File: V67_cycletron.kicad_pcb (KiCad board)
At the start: 4 copper layers, 107.8 x 44.1 mm, 54 parts, among them J1 USB_C_Receptacle_USB2.0_16P, J2 Conn_01x04_Socket, J3 Conn_01x04_Socket, U2 LM1117DT-3.3, U3 L7805, U4 ESP32-S3-WROOM-1

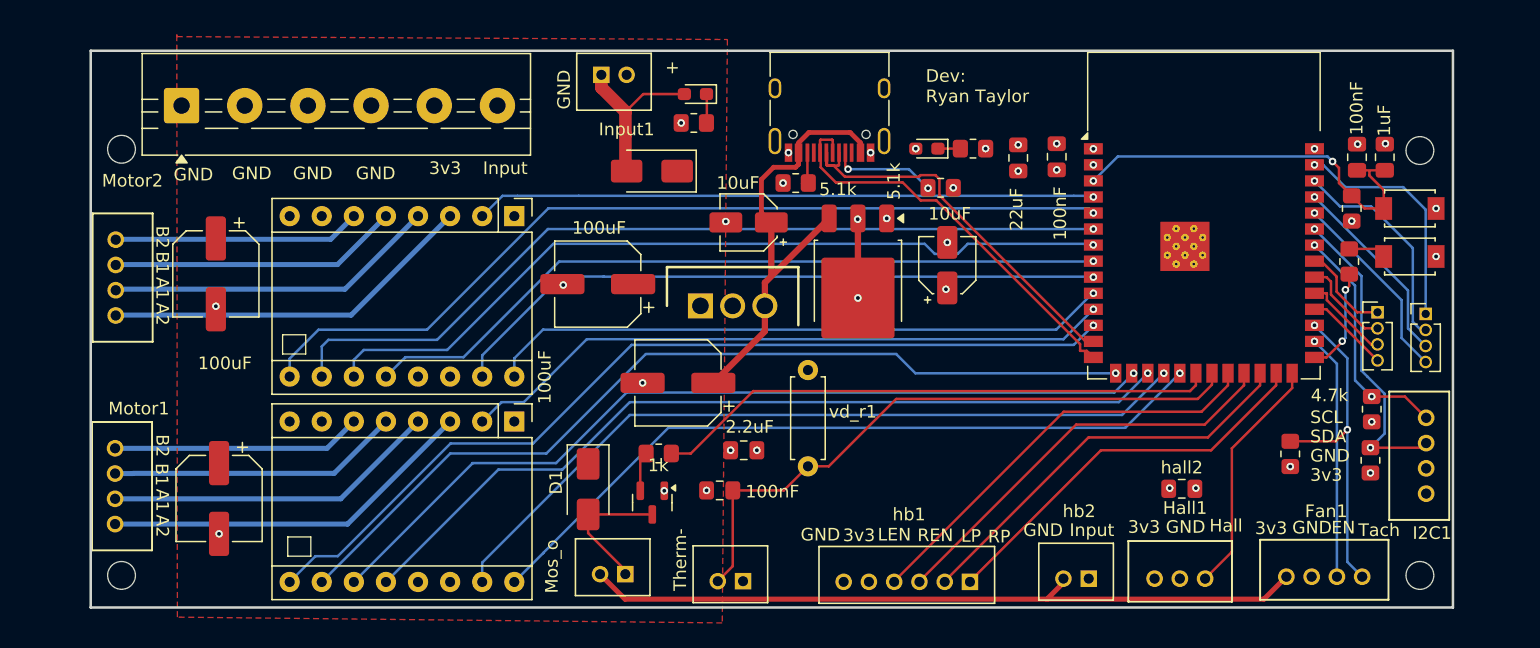
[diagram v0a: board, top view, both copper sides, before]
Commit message: change moving parts for reorder
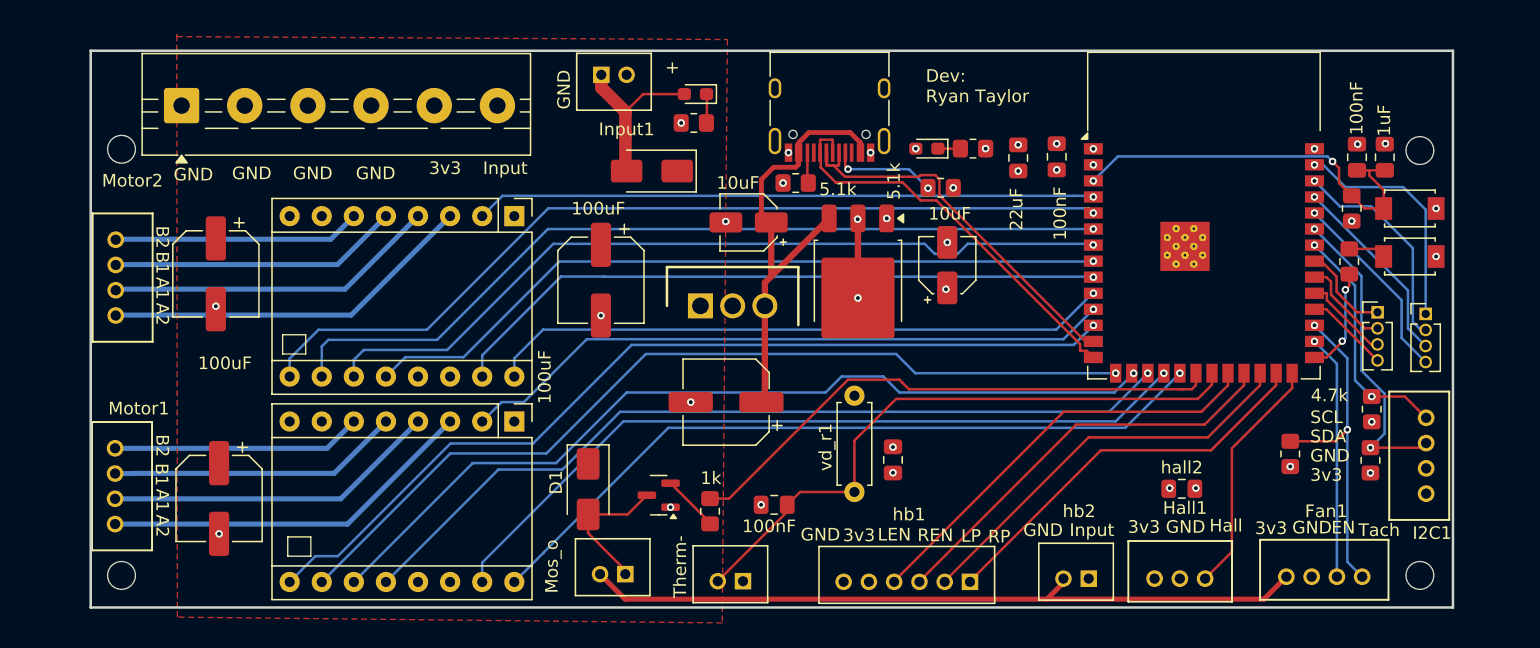
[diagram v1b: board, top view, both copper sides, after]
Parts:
- moved vd_c1 11.8 mm to (103.9, 104.9), turned to 90 degrees
- moved tr3 6.12 mm to (89.4, 109.0), turned to -90 degrees
- moved vd_c2 4.47 mm to (94.5, 108.5)
- moved vd_r1 4.21 mm to (100.8, 107.4)
- moved 3v3in1 4.10 mm to (90.7, 100.3)
- moved mosfet4 0.78 mm to (85.3, 107.7), turned to 180 degrees
- moved 5Vin1 0.40 mm to (80.8, 90.7), turned to -90 degrees
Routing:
- net Net-(mosfet4-G): track 3.31 -> 4.93 mm
- net Motor1_M1: track 68.6 -> 69.6 mm
- net mosfet1_i: track 44.7 -> 43.8 mm
- net Therm-: track 50.1 -> 49.3 mm
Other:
- board text removed: "2.2uF"

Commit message: updated for 3rd time, lcsc numbers for cap were through hole not smd, fixed
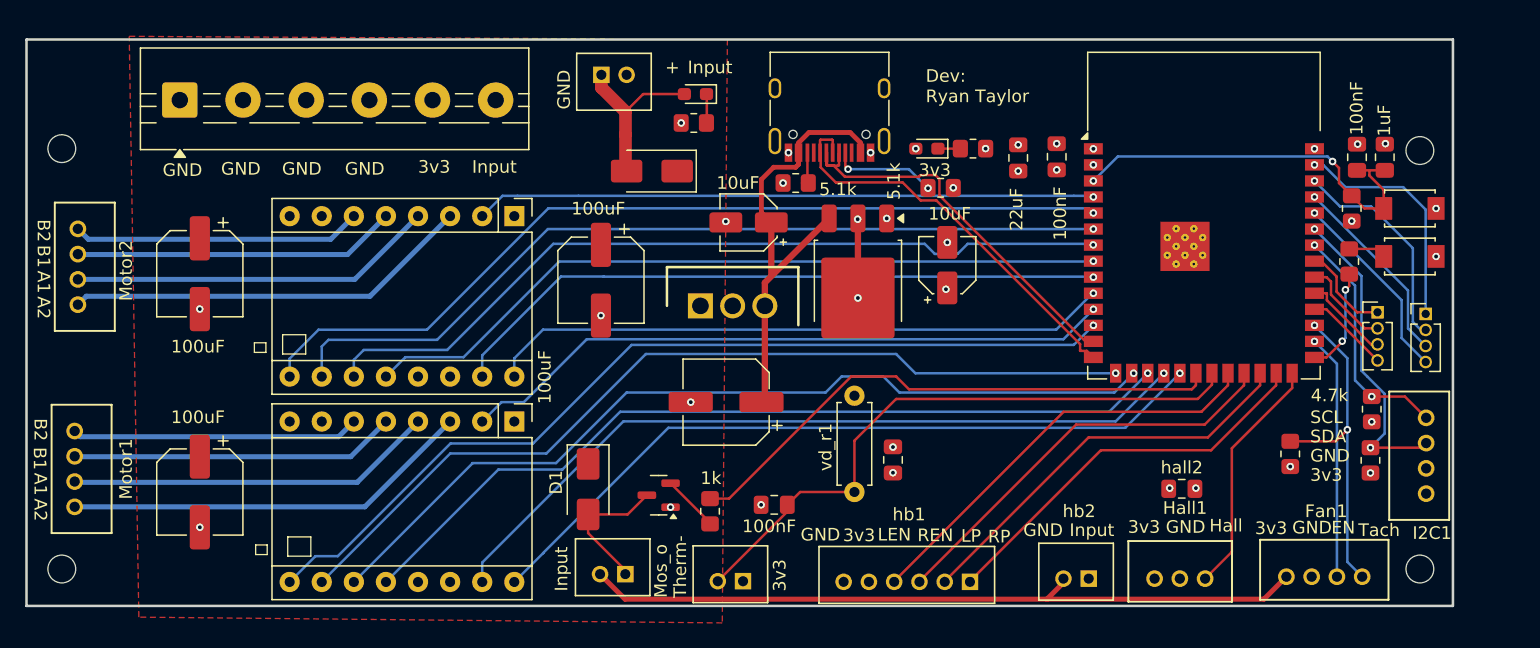
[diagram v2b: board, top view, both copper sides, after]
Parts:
- moved ? 4.75 mm to (38.1, 113.5)
- moved ? 4.72 mm to (38.1, 80.3)
- moved Motor1 3.48 mm to (39.1, 108.6)
- moved Motor2 3.12 mm to (39.4, 92.6)
- moved motorc1 1.61 mm to (49.0, 107.4)
- moved motorc2 1.27 mm to (49.0, 90.2)
- moved ? 0.51 mm to (145.6, 113.5)
- moved Rails1 0.46 mm to (47.4, 76.4)
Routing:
- net Motor2_B2: track 19.6 -> 22.9 mm
- net Motor1_B2: track 19.8 -> 22.8 mm
- net Motor2_A2: track 29.7 -> 32.6 mm
- net Motor2_B1: track 22.9 -> 25.7 mm
- net Motor2_A1: track 26.3 -> 29.0 mm
- net Motor1_A1: track 26.5 -> 29.2 mm
- net Motor1_A2: track 29.9 -> 32.5 mm
- net Motor1_B1: track 23.3 -> 25.8 mm
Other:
- board size 107.8 x 44.1 mm -> 112.9 x 44.8 mm

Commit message: update board test files, server connection,wifi, and some pcb changes
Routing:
- added copper zone on In2.Cu, net 3V3
- added copper zone on In1.Cu, net GND
- removed copper zone on In1.Cu, net 3V3
- removed copper zone on In2.Cu, net GND

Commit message: big changes to make it work
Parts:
- removed Fan1: PC_Fan, connector_4_vert:CONN4_B4B-PH_JST
- removed Hall1: Hall_Sens, connector_3_vert:CONN_B3B-PH-K-SLFSN_JST
- removed I2C1: MCP9600, connector_4_vert:CONN4_B4B-PH_JST
- removed Input1, Mos1, Therm1, hb2: B2B-PH-K-S, connector_2_vert:JST_B2B-PH-K-S
- removed Motor1: Motor1, connector_4_vert:CONN4_B4B-PH_JST
- removed Motor2: Motor2, connector_4_vert:CONN4_B4B-PH_JST
- removed hb1: B6B-PH-K-S, connector_6_vert:JST_B6B-PH-K-S
- removed mosfet4: HD2305, Package_TO_SOT_SMD:SOT-23
- added J10: Screw_Terminal_01x02, TerminalBlock:TerminalBlock_MaiXu_MX126-5.0-02P_1x02_P5.00mm, F.Cu at (80.0, 76.7)
- added J11: PINHD_1x2_Male, Connector_PinHeader_2.54mm:PinHeader_1x02_P2.54mm_Vertical, F.Cu at (150.6, 107.4)
- added J13: PINHD_2x2_Male, Connector_PinHeader_2.54mm:PinHeader_2x02_P2.54mm_Vertical, F.Cu at (145.2, 107.3)
- added J4: PINHD_1x4_Male, Connector_PinHeader_2.54mm:PinHeader_1x04_P2.54mm_Vertical, F.Cu at (150.5, 92.7)
- added J5: PINHD_1x4_Male, Connector_PinHeader_2.54mm:PinHeader_1x04_P2.54mm_Vertical, F.Cu at (40.0, 94.1)
- added J6: PINHD_1x4_Male, Connector_PinHeader_2.54mm:PinHeader_1x04_P2.54mm_Vertical, F.Cu at (40.0, 109.8)
- added J7: PINHD_1x4_Male, Connector_PinHeader_2.54mm:PinHeader_1x04_P2.54mm_Vertical, F.Cu at (138.9, 114.1)
- added J8: PINHD_2x4_Male, Connector_PinHeader_2.54mm:PinHeader_2x04_P2.54mm_Vertical, F.Cu at (106.9, 114.4)
- added J9: PINHD_1x3_Male, Connector_PinHeader_2.54mm:PinHeader_1x03_P2.54mm_Vertical, F.Cu at (120.7, 114.4)
- added Q1: IRF1324, PCM_Package_TO_SOT_THT_AKL:TO-220-3_Vertical_GDS, F.Cu at (97.7, 111.2)
- D4, D5: value LED -> LED_RED
- J2, J3: value Conn_01x04_Socket -> PINHD_1x2_Male; footprint Connector_PinHeader_1.27mm:PinHeader_1x04_P1.27mm_Vertical -> Connector_PinHeader_2.54mm:PinHeader_1x02_P2.54mm_Vertical
- moved J3 62.7 mm to (83.4, 114.8), turned to -90 degrees
- moved vd_c2 38.7 mm to (133.2, 107.8)
- moved vd_r1 38.2 mm to (138.6, 101.5), turned to 180 degrees
- moved vd_c1 28.7 mm to (131.8, 111.5), turned to 180 degrees
- moved J2 25.2 mm to (132.3, 114.5), turned to -90 degrees
- moved 5Vout1 14.5 mm to (93.8, 100.5)
- moved 3v3out1 12.7 mm to (101.6, 100.3), turned to 180 degrees
- moved tr3 12.4 mm to (101.7, 107.6), turned to 0 degrees
- moved hall2 11.1 mm to (117.5, 113.2), turned to 90 degrees
- moved R_En1 10.3 mm to (150.5, 85.2), turned to 180 degrees
- moved R_boot1 9.23 mm to (149.2, 88.4), turned to 90 degrees
- moved R5 8.98 mm to (147.0, 97.7)
- moved R4 8.82 mm to (146.9, 93.7)
- moved 3v3in1 7.98 mm to (82.8, 101.2)
- moved R7 7.37 mm to (138.0, 111.3), turned to 0 degrees
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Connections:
- J2 pad 1: IO1 -> 3V3
- J2 pad 2: IO2 -> Therm-
- J3 pad 1: IO40 -> mosfet1_o
- J3 pad 2: IO39 -> +24V
- U4 pad 21: Therm- -> R_IS
- U4 pad 22: L_EN -> L_IS
- U4 pad 24: LPWM -> L_EN
- U4 pad 26: Hall_i -> unconnected-(U4-IO45-Pad26)
- U4 pad 28: FAN_En_o -> LPWM
- U4 pad 29: FAN_Tach_i -> Hall_i
- U4 pad 30: IO37 -> Therm-
- U4 pad 31: IO38 -> FAN_Tach_i
- U4 pad 32: IO39 -> FAN_En_o
- U4 pad 33: IO40 -> Heat_o
- U4 pad 34: SCL -> SDA
- U4 pad 35: SDA -> SCL
- tr3 pad 1: mosfet1_i -> Net-(Q1-G)
- tr3 pad 2: Net-(mosfet4-G) -> mosfet1_i
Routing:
- net L_IS: track 0.00 -> 29.4 mm
- net R_IS: track 0.00 -> 26.2 mm
- net BOOT: track 8.71 -> 34.3 mm
- net Heat_o: track 0.00 -> 21.8 mm
- net Therm-: track 49.3 -> 27.7 mm
- net mosfet1_i: track 44.0 -> 30.0 mm
- net +5V: track 36.3 -> 49.1 mm
- net Hall_i: track 19.1 -> 31.8 mm
- net IO2: track 17.1 -> 28.7 mm
- net IO1: track 18.5 -> 27.4 mm
- net RX: track 15.4 -> 24.2 mm
- net TX: track 15.4 -> 22.9 mm
- net IO40: track 7.37 -> 0.00 mm
- net IO39: track 7.27 -> 0.00 mm
- net FAN_En_o: track 19.4 -> 26.5 mm, vias 1 -> 0
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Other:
- board size 112.9 x 44.8 mm -> 117.7 x 44.2 mm
- board text added: "-"
- board text added: "3v3 RIS REN RP GND LIS LEN LP"
- board text added: "Gnd Heat"
- board text added: "Hall GND 3v3"
- board text added: "Tac En Gnd In"
- board text removed: "EN"
- board text removed: "Hall"
- board text removed: "LEN"
- board text removed: "LP"
- board text removed: "Mos_o"
- board text removed: "REN"
- board text removed: "RP"
- board text removed: "Tach"
- board text removed: "Therm-"

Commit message: changes to pin placement
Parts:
- removed J13: PINHD_2x2_Male, Connector_PinHeader_2.54mm:PinHeader_2x02_P2.54mm_Vertical
- added J12: PINHD_1x2_Male, Connector_PinHeader_2.54mm:PinHeader_1x02_P2.54mm_Vertical, F.Cu at (145.2, 104.7)
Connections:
- U4 pad 26: unconnected-(U4-IO45-Pad26) -> LPWM
- U4 pad 28: LPWM -> unconnected-(U4-IO35-Pad28)
- U4 pad 29: Hall_i -> unconnected-(U4-IO36-Pad29)
- U4 pad 30: Therm- -> unconnected-(U4-IO37-Pad30)
- U4 pad 38: IO2 -> Hall_i
- U4 pad 39: IO1 -> Therm-
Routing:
- net IO2: track 28.7 -> 0.00 mm, vias 1 -> 0
- net IO1: track 27.4 -> 0.00 mm, vias 1 -> 0
- net Hall_i: track 31.8 -> 42.3 mm, vias 0 -> 1
- net Therm-: track 27.7 -> 38.0 mm, vias 0 -> 1
- net LPWM: track 34.6 -> 28.5 mm, vias 0 -> 1
- net TX: track 22.9 -> 25.5 mm
- net RX: track 24.2 -> 26.3 mm
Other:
- board text added: "Tac PWM Gnd In"
- board text removed: "Tac En Gnd In"
